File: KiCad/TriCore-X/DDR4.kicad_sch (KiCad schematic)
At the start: 0 parts

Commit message: feat : add some Expansion Ports (work in progress)
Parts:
- added U1: RK3568B2, RK3568B2:BGA636C65P28X28_1900X1900X111, symbol RK3568B2:RK3568B2
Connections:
- new net DDR_DQ0_A: U1.F2 (DDR_DQ0_A)
- new net DDR_DQ0_B: U1.B10 (DDR_DQ0_B)
- new net DDR_DQ10_A: U1.L7 (DDR_DQ10_A)
- new net DDR_DQ10_B: U1.A17 (DDR_DQ10_B)
- new net DDR_DQ11_A: U1.L6 (DDR_DQ11_A)
- new net DDR_DQ11_B: U1.B18 (DDR_DQ11_B)
- new net DDR_DQ12_A: U1.K2 (DDR_DQ12_A)
- new net DDR_DQ12_B: U1.B13 (DDR_DQ12_B)
- new net DDR_DQ13_A: U1.J6 (DDR_DQ13_A)
- new net DDR_DQ13_B: U1.A13 (DDR_DQ13_B)
- new net DDR_DQ14_A: U1.J7 (DDR_DQ14_A)
- new net DDR_DQ14_B: U1.D17 (DDR_DQ14_B)
- new net DDR_DQ15_A: U1.L4 (DDR_DQ15_A)
- new net DDR_DQ15_B: U1.B14 (DDR_DQ15_B)
- new net DDR_DQ1_A: U1.E1 (DDR_DQ1_A)
- new net DDR_DQ1_B: U1.A9 (DDR_DQ1_B)
- new net DDR_DQ2_A: U1.E2 (DDR_DQ2_A)
- new net DDR_DQ2_B: U1.D12 (DDR_DQ2_B)
- new net DDR_DQ3_A: U1.D1 (DDR_DQ3_A)
- new net DDR_DQ3_B: U1.E12 (DDR_DQ3_B)
- new net DDR_DQ4_A: U1.J1 (DDR_DQ4_A)
- new net DDR_DQ4_B: U1.A12 (DDR_DQ4_B)
- new net DDR_DQ5_A: U1.J2 (DDR_DQ5_A)
- new net DDR_DQ5_B: U1.D15 (DDR_DQ5_B)
- new net DDR_DQ6_A: U1.H1 (DDR_DQ6_A)
- new net DDR_DQ6_B: U1.E15 (DDR_DQ6_B)
- new net DDR_DQ7_A: U1.H4 (DDR_DQ7_A)
- new net DDR_DQ7_B: U1.E14 (DDR_DQ7_B)
- new net DDR_DQ8_A: U1.M1 (DDR_DQ8_A)
- new net DDR_DQ8_B: U1.A16 (DDR_DQ8_B)
- new net DDR_DQ9_A: U1.N2 (DDR_DQ9_A)
- new net DDR_DQ9_B: U1.B17 (DDR_DQ9_B)

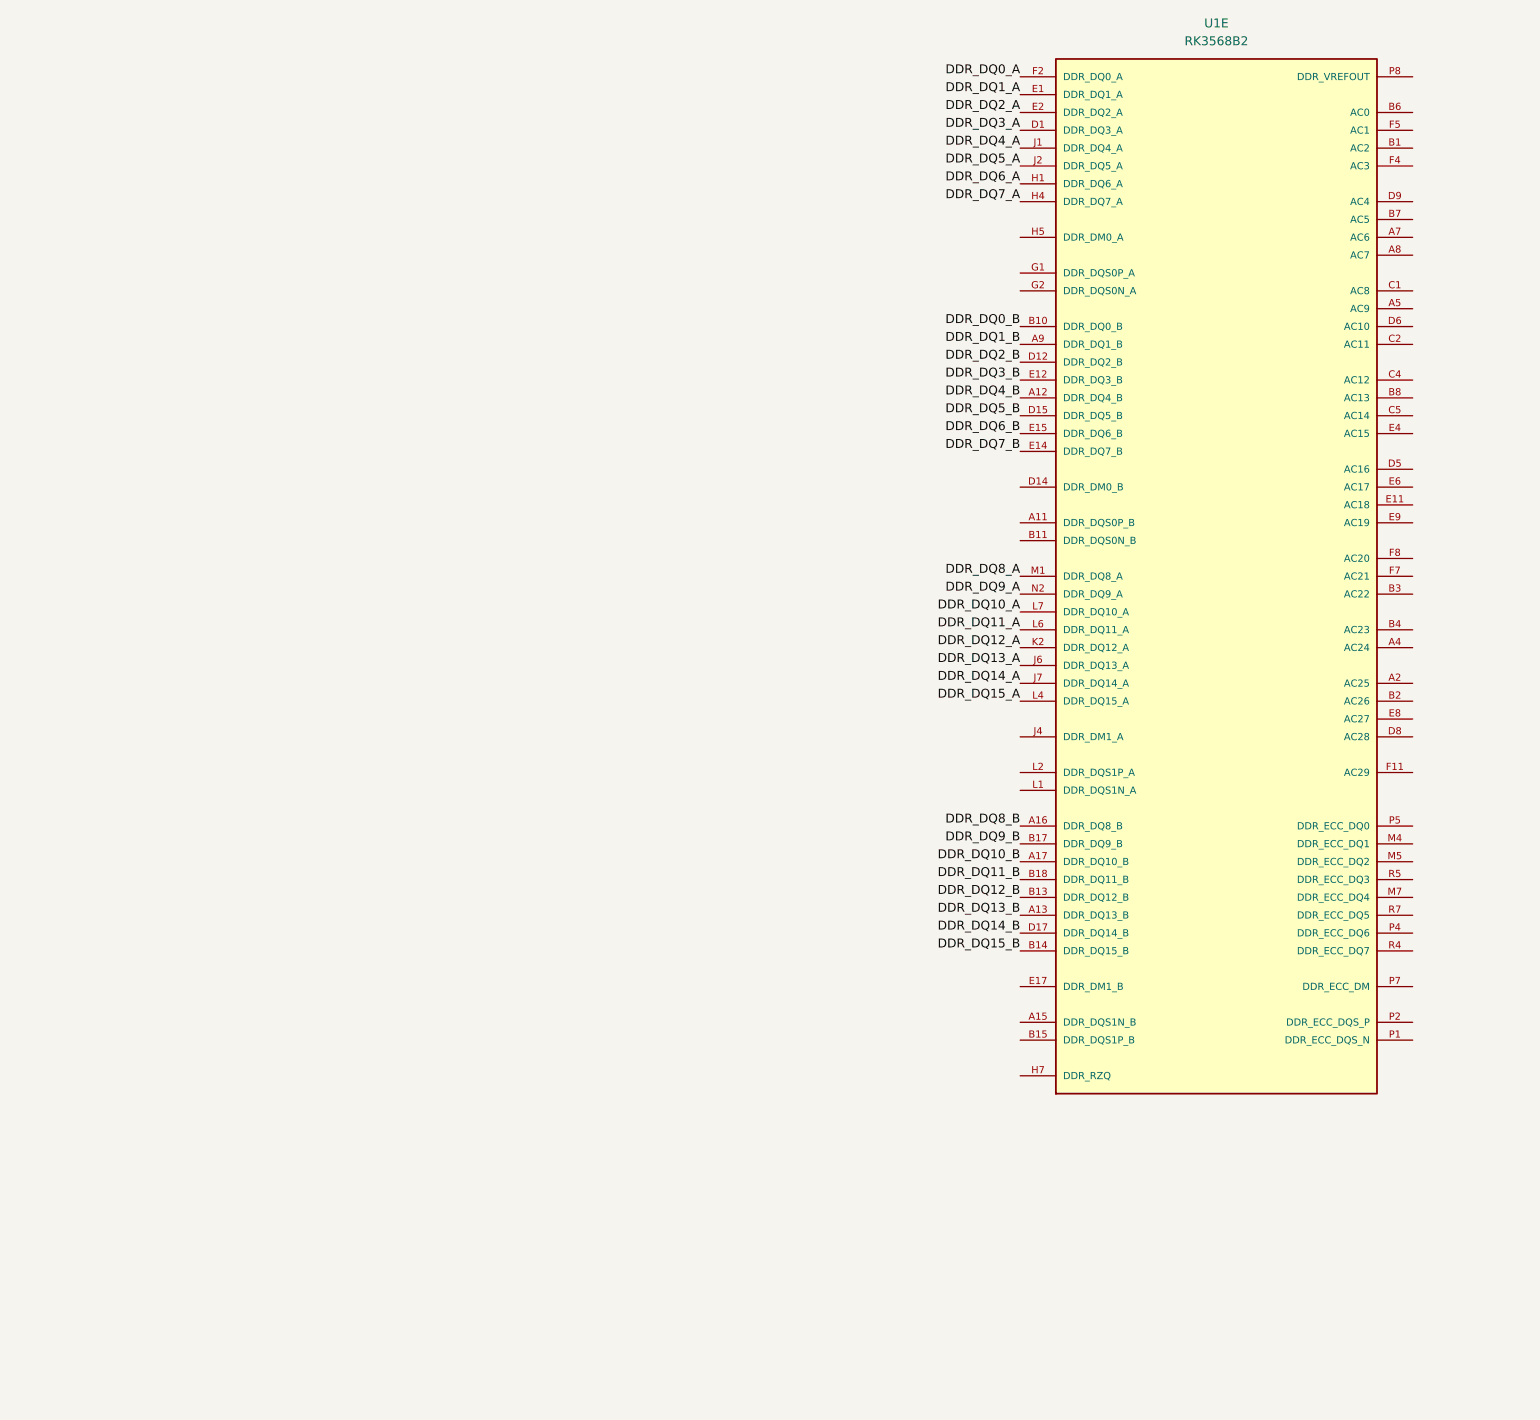
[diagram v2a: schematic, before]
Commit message: refactor: change core MCU to STM32H723 and add LPDDR4/HDMI support
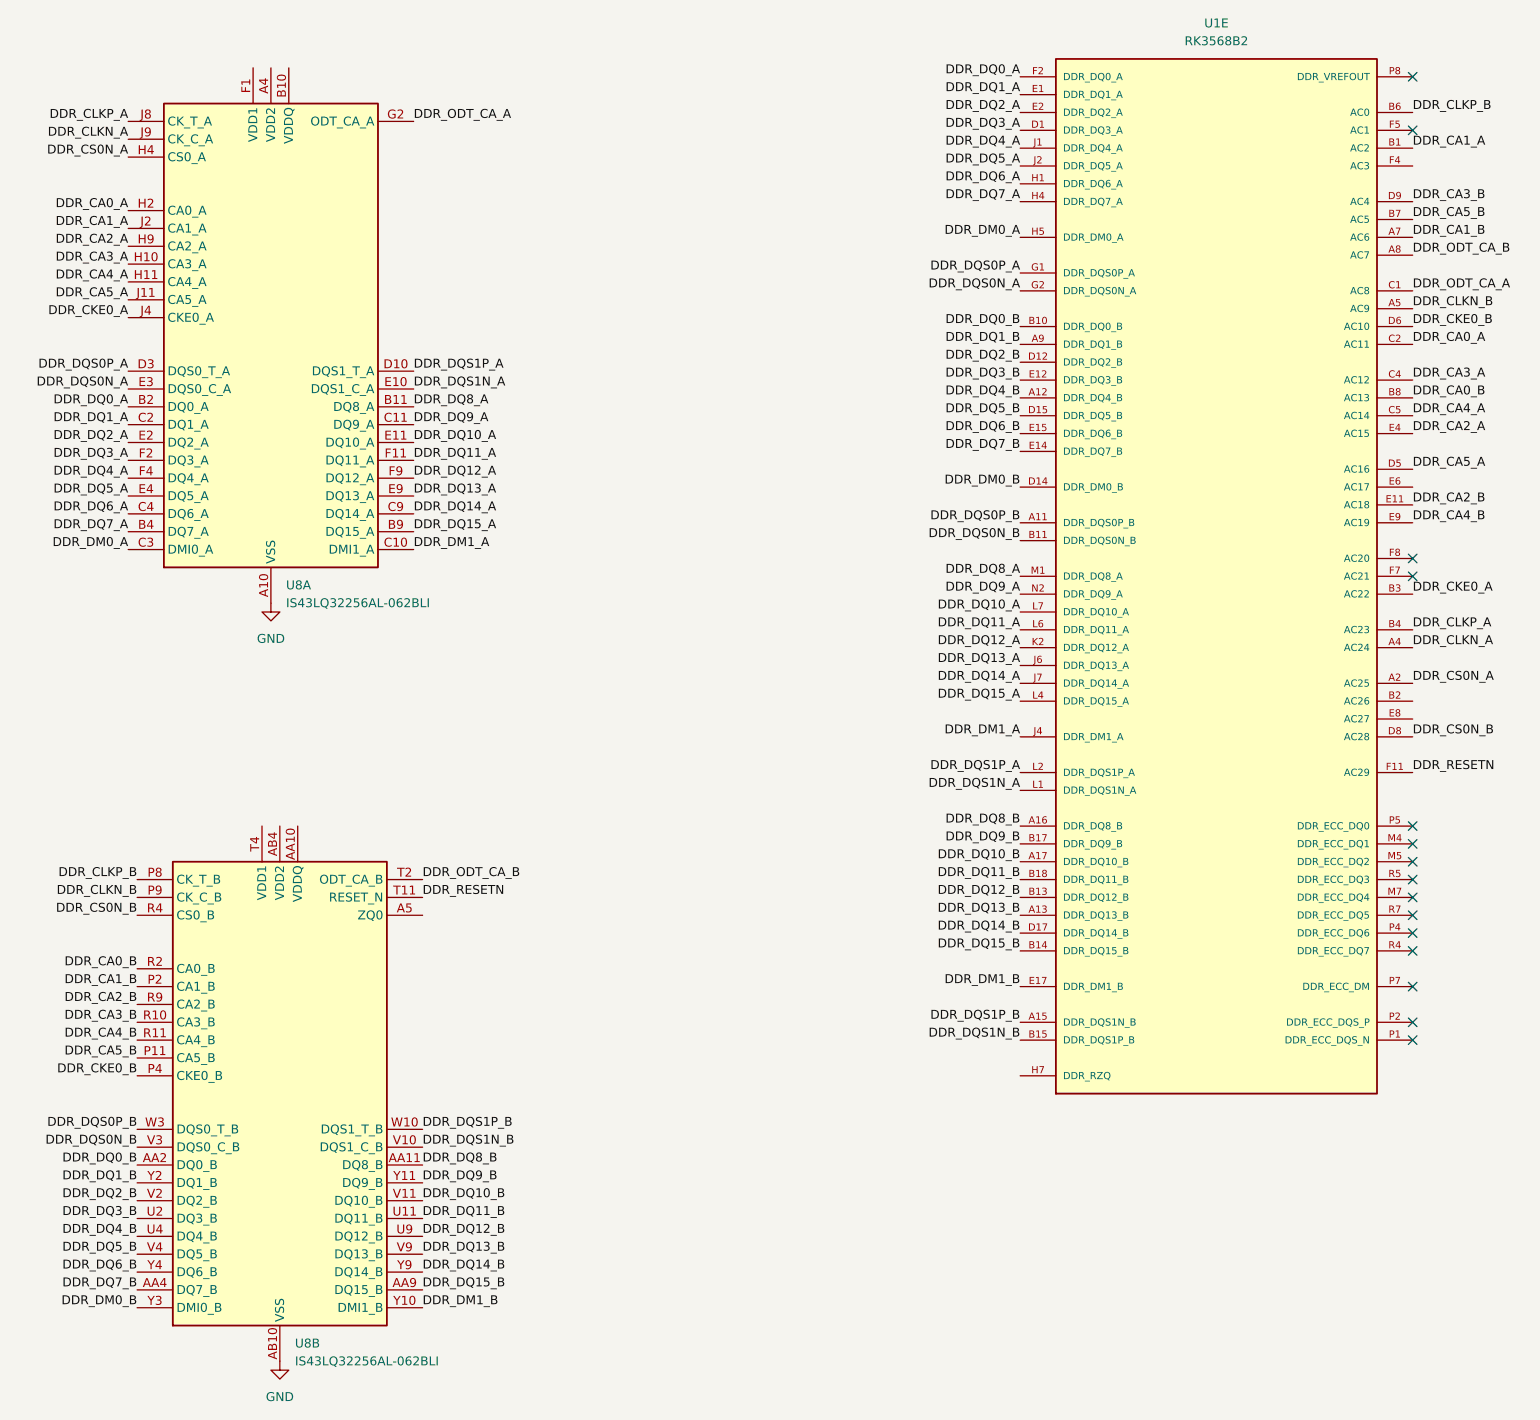
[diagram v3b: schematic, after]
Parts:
- added U8: IS43LQ32256AL-062BLI, Package_BGA:BGA-200_10x14.5mm_Layout12x22_P0.8x0.65mm, symbol Memory_RAM:IS43LQ32256AL-062BLI
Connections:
- net DDR_DQ0_A: now also U8.B2 (DQ0_A)
- net DDR_DQ0_B: now also U8.AA2 (DQ0_B)
- net DDR_DQ10_A: now also U8.E11 (DQ10_A)
- net DDR_DQ10_B: now also U8.V11 (DQ10_B)
- net DDR_DQ11_A: now also U8.F11 (DQ11_A)
- net DDR_DQ11_B: now also U8.U11 (DQ11_B)
- net DDR_DQ12_A: now also U8.F9 (DQ12_A)
- net DDR_DQ12_B: now also U8.U9 (DQ12_B)
- net DDR_DQ13_A: now also U8.E9 (DQ13_A)
- net DDR_DQ13_B: now also U8.V9 (DQ13_B)
- net DDR_DQ14_A: now also U8.C9 (DQ14_A)
- net DDR_DQ14_B: now also U8.Y9 (DQ14_B)
- net DDR_DQ15_A: now also U8.B9 (DQ15_A)
- net DDR_DQ15_B: now also U8.AA9 (DQ15_B)
- net DDR_DQ1_A: now also U8.C2 (DQ1_A)
- net DDR_DQ1_B: now also U8.Y2 (DQ1_B)
- net DDR_DQ2_A: now also U8.E2 (DQ2_A)
- net DDR_DQ2_B: now also U8.V2 (DQ2_B)
- net DDR_DQ3_A: now also U8.F2 (DQ3_A)
- net DDR_DQ3_B: now also U8.U2 (DQ3_B)
- net DDR_DQ4_A: now also U8.F4 (DQ4_A)
- net DDR_DQ4_B: now also U8.U4 (DQ4_B)
- net DDR_DQ5_A: now also U8.E4 (DQ5_A)
- net DDR_DQ5_B: now also U8.V4 (DQ5_B)
- net DDR_DQ6_A: now also U8.C4 (DQ6_A)
- net DDR_DQ6_B: now also U8.Y4 (DQ6_B)
- net DDR_DQ7_A: now also U8.B4 (DQ7_A)
- net DDR_DQ7_B: now also U8.AA4 (DQ7_B)
- net DDR_DQ8_A: now also U8.B11 (DQ8_A)
- net DDR_DQ8_B: now also U8.AA11 (DQ8_B)
- net DDR_DQ9_A: now also U8.C11 (DQ9_A)
- net DDR_DQ9_B: now also U8.Y11 (DQ9_B)
- net DDR_DQS0P_B: now reaches U1.A11 (DDR_DQS0P_B)
- net DDR_DQS0P_B: now also U8.W3 (DQS0_T_B)
- net DDR_DQS1P_B: now reaches U1.A15 (DDR_DQS1N_B)
- net DDR_DQS1P_B: now also U8.W10 (DQS1_T_B)
- net DDR_CS0N_A: now reaches U1.A2 (AC25)
- net DDR_CS0N_A: now also U8.H4 (CS0_A)
- net DDR_CLKN_A: now reaches U1.A4 (AC24)
- net DDR_CLKN_A: now also U8.J9 (CK_C_A)
- net DDR_CLKN_B: now reaches U1.A5 (AC9)
- net DDR_CLKN_B: now also U8.P9 (CK_C_B)
- net DDR_CA1_B: now reaches U1.A7 (AC6)
- net DDR_CA1_B: now also U8.P2 (CA1_B)
- net DDR_ODT_CA_B: now reaches U1.A8 (AC7)
- net DDR_ODT_CA_B: now also U8.T2 (ODT_CA_B)
- net DDR_CA1_A: now reaches U1.B1 (AC2)
- net DDR_CA1_A: now also U8.J2 (CA1_A)
- net DDR_DQS0N_B: now reaches U1.B11 (DDR_DQS0N_B)
- net DDR_DQS0N_B: now also U8.V3 (DQS0_C_B)
- net DDR_DQS1N_B: now reaches U1.B15 (DDR_DQS1P_B)
- net DDR_DQS1N_B: now also U8.V10 (DQS1_C_B)
- net DDR_CKE0_A: now reaches U1.B3 (AC22)
- net DDR_CKE0_A: now also U8.J4 (CKE0_A)
- net DDR_CLKP_A: now reaches U1.B4 (AC23)
- net DDR_CLKP_A: now also U8.J8 (CK_T_A)
- net DDR_CLKP_B: now reaches U1.B6 (AC0)
- net DDR_CLKP_B: now also U8.P8 (CK_T_B)
- net DDR_CA5_B: now reaches U1.B7 (AC5)
- net DDR_CA5_B: now also U8.P11 (CA5_B)
- net DDR_CA0_B: now reaches U1.B8 (AC13)
- net DDR_CA0_B: now also U8.R2 (CA0_B)
- net DDR_ODT_CA_A: now reaches U1.C1 (AC8)
- net DDR_ODT_CA_A: now also U8.G2 (ODT_CA_A)
- net DDR_CA0_A: now reaches U1.C2 (AC11)
- net DDR_CA0_A: now also U8.H2 (CA0_A)
- net DDR_CA3_A: now reaches U1.C4 (AC12)
- net DDR_CA3_A: now also U8.H10 (CA3_A)
- net DDR_CA4_A: now reaches U1.C5 (AC14)
- net DDR_CA4_A: now also U8.H11 (CA4_A)
- net DDR_DM0_B: now reaches U1.D14 (DDR_DM0_B)
- net DDR_DM0_B: now also U8.Y3 (DMI0_B)
- net DDR_CA5_A: now reaches U1.D5 (AC16)
- net DDR_CA5_A: now also U8.J11 (CA5_A)
- net DDR_CKE0_B: now reaches U1.D6 (AC10)
- net DDR_CKE0_B: now also U8.P4 (CKE0_B)
- net DDR_CS0N_B: now reaches U1.D8 (AC28)
- net DDR_CS0N_B: now also U8.R4 (CS0_B)
- net DDR_CA3_B: now reaches U1.D9 (AC4)
- net DDR_CA3_B: now also U8.R10 (CA3_B)
- net DDR_CA2_B: now reaches U1.E11 (AC18)
- net DDR_CA2_B: now also U8.R9 (CA2_B)
- net DDR_DM1_B: now reaches U1.E17 (DDR_DM1_B)
- net DDR_DM1_B: now also U8.Y10 (DMI1_B)
- net DDR_CA2_A: now reaches U1.E4 (AC15)
- net DDR_CA2_A: now also U8.H9 (CA2_A)
- net DDR_CA4_B: now reaches U1.E9 (AC19)
- net DDR_CA4_B: now also U8.R11 (CA4_B)
- net DDR_RESETN: now reaches U1.F11 (AC29)
- net DDR_RESETN: now also U8.T11 (RESET_N)
- net DDR_DQS0P_A: now reaches U1.G1 (DDR_DQS0P_A)
- net DDR_DQS0P_A: now also U8.D3 (DQS0_T_A)
- net DDR_DQS0N_A: now reaches U1.G2 (DDR_DQS0N_A)
- net DDR_DQS0N_A: now also U8.E3 (DQS0_C_A)
- net DDR_DM0_A: now reaches U1.H5 (DDR_DM0_A)
- net DDR_DM0_A: now also U8.C3 (DMI0_A)
- net DDR_DM1_A: now reaches U1.J4 (DDR_DM1_A)
- net DDR_DM1_A: now also U8.C10 (DMI1_A)
- net DDR_DQS1N_A: now reaches U1.L1 (DDR_DQS1N_A)
- net DDR_DQS1N_A: now also U8.E10 (DQS1_C_A)
- net DDR_DQS1P_A: now reaches U1.L2 (DDR_DQS1P_A)
- net DDR_DQS1P_A: now also U8.D10 (DQS1_T_A)
- new net: U8.AA10 (VDDQ), U8.AA3 (VDDQ), U8.AA5 (VDDQ), U8.AA8 (VDDQ), U8.U10 (VDDQ), U8.U3 (VDDQ), U8.W1 (VDDQ), U8.W12 (VDDQ), U8.W5 (VDDQ), U8.W8 (VDDQ)
- new net: U8.AB4 (VDD2), U8.AB9 (VDD2), U8.N1 (VDD2), U8.N10 (VDD2), U8.N12 (VDD2), U8.N3 (VDD2), U8.R1 (VDD2), U8.R12 (VDD2), U8.R5 (VDD2), U8.R8 (VDD2), U8.U5 (VDD2), U8.U8 (VDD2)
- new net: U8.T4 (VDD1), U8.T9 (VDD1), U8.U1 (VDD1), U8.U12 (VDD1)
- new net: U8.A4 (VDD2), U8.A9 (VDD2), U8.F5 (VDD2), U8.F8 (VDD2), U8.H1 (VDD2), U8.H12 (VDD2), U8.H5 (VDD2), U8.H8 (VDD2), U8.K1 (VDD2), U8.K10 (VDD2), U8.K12 (VDD2), U8.K3 (VDD2)
- new net: U8.B10 (VDDQ), U8.B3 (VDDQ), U8.B5 (VDDQ), U8.B8 (VDDQ), U8.D1 (VDDQ), U8.D12 (VDDQ), U8.D5 (VDDQ), U8.D8 (VDDQ), U8.F10 (VDDQ), U8.F3 (VDDQ)
- new net: U8.F1 (VDD1), U8.F12 (VDD1), U8.G4 (VDD1), U8.G9 (VDD1)
- new net GND: U8.A10 (VSS), U8.A3 (VSS), U8.AB10 (VSS), U8.AB3 (VSS), U8.AB5 (VSS), U8.AB8 (VSS), U8.C1 (VSS), U8.C12 (VSS), U8.C5 (VSS), U8.C8 (VSS), U8.D11 (VSS), U8.D2 (VSS), U8.D4 (VSS), U8.D9 (VSS), U8.E1 (VSS), U8.E12 (VSS), U8.E5 (VSS), U8.E8 (VSS), U8.G1 (VSS), U8.G10 (VSS), U8.G12 (VSS), U8.G3 (VSS), U8.G5 (VSS), U8.G8 (VSS), U8.J1 (VSS), U8.J10 (VSS), U8.J12 (VSS), U8.J3 (VSS), U8.K11 (VSS), U8.K2 (VSS), U8.K4 (VSS), U8.K9 (VSS), U8.N11 (VSS), U8.N2 (VSS), U8.N4 (VSS), U8.N9 (VSS), U8.P1 (VSS), U8.P10 (VSS), U8.P12 (VSS), U8.P3 (VSS), U8.T1 (VSS), U8.T10 (VSS), U8.T12 (VSS), U8.T3 (VSS), U8.T5 (VSS), U8.T8 (VSS), U8.V1 (VSS), U8.V12 (VSS), U8.V5 (VSS), U8.V8 (VSS), U8.W11 (VSS), U8.W2 (VSS), U8.W4 (VSS), U8.W9 (VSS), U8.Y1 (VSS), U8.Y12 (VSS), U8.Y5 (VSS), U8.Y8 (VSS)
- no-connect marks 0 -> 15
